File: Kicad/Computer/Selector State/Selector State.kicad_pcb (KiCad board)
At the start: 2 copper layers, 61 x 61 mm, 62 parts, among them IC1 FAN2558S38X, IC10 74LVC257AD,118, IC11 74LVC257AD,118, IC2 74LVC32APW,118, IC3 74LVC32APW,118, IC4 74LVC595APW, IC5 SN74ALVC08PWR, IC6 SN74ABT245BDBR, IC7 SN74ABT245BDBR, IC8 74ALVC04PW,118, IC9 74ALVC00PW,118, J1 Conn_01x02_Male, J10 Conn_01x02_Male, J11 Conn_01x10_Male, J12 Conn_01x02_Male, J2 Conn_01x12_Male, J3 Conn_01x02_Male, J4 Conn_01x02_Male, J5 Conn_01x12_Male, J6 Conn_01x02_Male, J7 Conn_01x02_Male, J8 Conn_01x10_Male, J9 Conn_01x02_Male

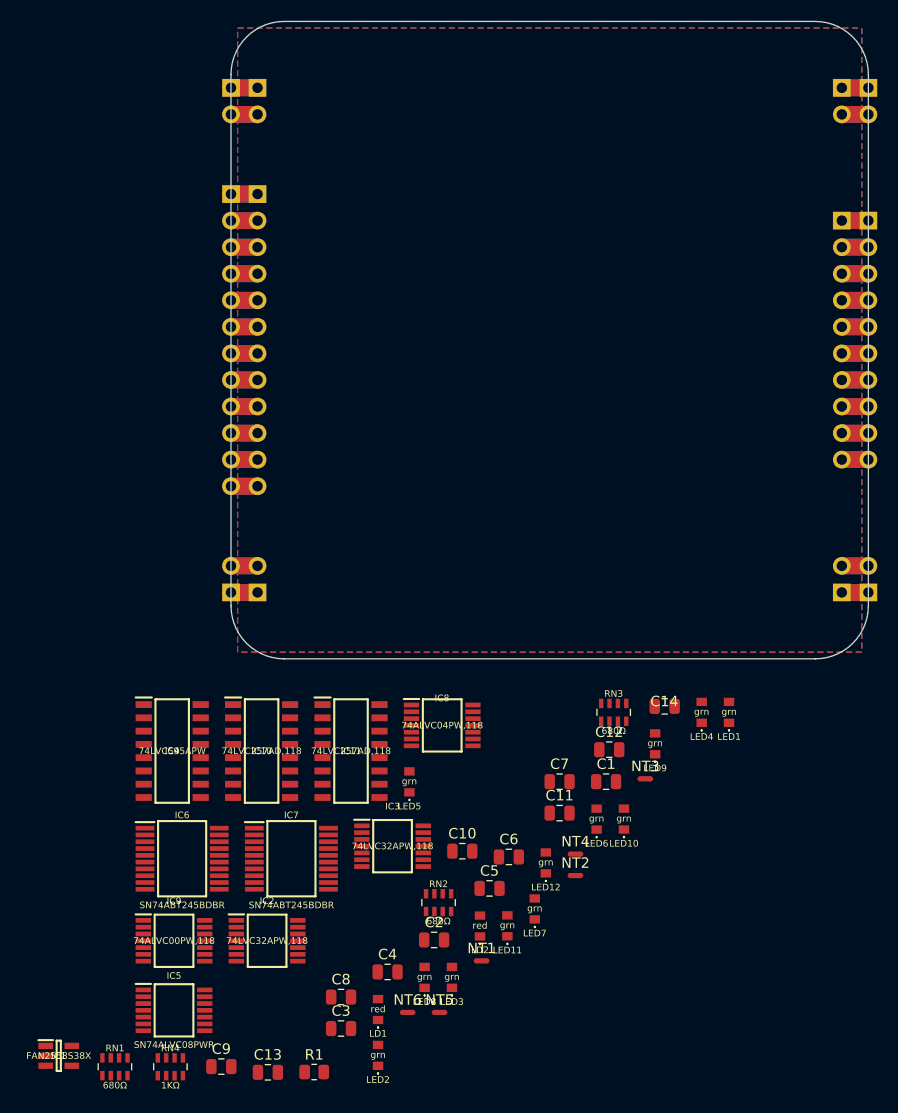
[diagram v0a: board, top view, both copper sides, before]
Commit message: Began routing Selector.
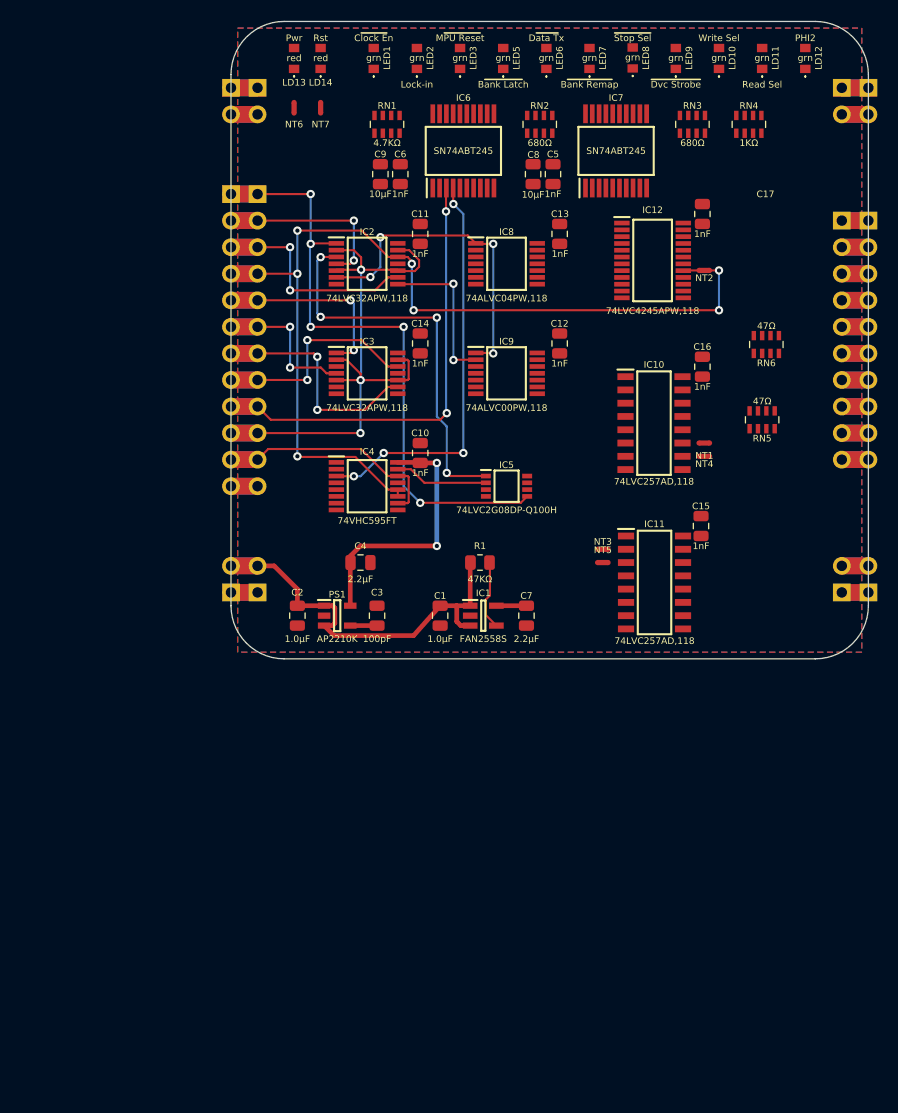
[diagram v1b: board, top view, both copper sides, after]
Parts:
- removed LD1, LD2: 150224SS73100, SamacSys_Parts:150224SS73100A
- removed LED10, LED11, LED12, LED4: 150224VS73100A, SamacSys_Parts:150224VS73100A
- added C15: C_Small, Capacitor_SMD:C_0805_2012Metric, F.Cu at (187.2, 85.1)
- added C16: C_Small, Capacitor_SMD:C_0805_2012Metric, F.Cu at (187.3, 69.8)
- added C17: C_Small, Capacitor_SMD:C_0805_2012Metric, F.Cu at (187.3, 55.2)
- added IC12: 74LVC4245APW,118, SamacSys_Parts:SOP65P640X110-24N, F.Cu at (182.6, 59.7)
- added LD10: 150224VS73100A, SamacSys_Parts:150224VS73100A, F.Cu at (188.9, 40.4)
- added LD11: 150224VS73100A, SamacSys_Parts:150224VS73100A, F.Cu at (193.0, 40.4)
- added LD12: 150224VS73100A, SamacSys_Parts:150224VS73100A, F.Cu at (197.2, 40.4)
- added LD13: 150224SS73100, SamacSys_Parts:150224SS73100A, F.Cu at (148.3, 40.4)
- added LD14: 150224SS73100, SamacSys_Parts:150224SS73100A, F.Cu at (150.8, 40.4)
- added NT7: NetTie_2, NetTie:NetTie-2_SMD_Pad0.5mm, F.Cu at (150.8, 45.1)
- added PS1: AP2210K-5.0TRG1, SamacSys_Parts:SOT95P282X130-5N, F.Cu at (152.4, 93.7)
- added RN5: CAY16-470J4LF, SamacSys_Parts:CAY16470J4LF, F.Cu at (193.0, 74.9)
- added RN6: CAY16-470J4LF, SamacSys_Parts:CAY16470J4LF, F.Cu at (193.4, 67.7)
- IC4: value 74LVC595APW -> 74VHC595FT; footprint SamacSys_Parts:SOIC127P600X175-16N -> SamacSys_Parts:SOP65P640X120-16N
- IC5: value SN74ALVC08PWR -> 74LVC2G08DP-Q100H; footprint SamacSys_Parts:SOP65P640X120-14N -> SamacSys_Parts:SOP65P400X110-8N
- IC6, IC7: value SN74ABT245BDBR -> SN74ABT245
- RN1: value CAY16-681J4LF -> CAY16-472J4LF
- moved RN4 105.8 mm to (191.8, 46.7)
- moved LED2 95.4 mm to (160.0, 40.4)
- moved RN1 93.8 mm to (157.2, 46.7)
- moved LED8 90.2 mm to (180.7, 40.3)
- moved LED3 87.9 mm to (164.1, 40.4)
- moved NT6 87.2 mm to (148.3, 45.1), turned to 90 degrees
- moved C9 86.7 mm to (156.5, 51.4), turned to 90 degrees
- moved C13 84.9 mm to (173.7, 57.1), turned to -90 degrees
- moved LED7 81.5 mm to (176.5, 40.4)
- moved C8 80.8 mm to (171.1, 51.4), turned to 90 degrees
- moved RN2 75.1 mm to (171.8, 46.7)
- moved IC7 74.5 mm to (179.1, 49.2), turned to 90 degrees
- moved LED6 72.9 mm to (172.4, 40.4)
- moved IC6 72.8 mm to (164.5, 49.2), turned to 90 degrees
- moved LED1 71.2 mm to (155.9, 40.4)
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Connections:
- net Net-(IC2-Pad6) renamed /Select 1 ^{AND} Enable
- net Net-(IC2-Pad8) renamed /Select 2 ^{AND} Enable
- net Net-(IC3-Pad11) renamed /Select 7 ^{AND} Enable
- net Net-(IC3-Pad3) renamed /Select 4 ^{AND} Enable
- net Net-(IC3-Pad6) renamed /Select 5 ^{AND} Enable
- net Net-(IC3-Pad8) renamed /Select 6 ^{AND} Enable
- C10 pad 2: VCC -> 5V
- C11 pad 2: VCC -> 3V
- C12 pad 2: VCC -> 3V
- C13 pad 2: VCC -> 3V
- C14 pad 2: VCC -> 3V
- C2 pad 2: VCC -> /Source 5V
- C3 pad 2: VCC -> Net-(C3-Pad2)
- C4 pad 2: VCC -> 5V
- C5 pad 2: VCC -> 5V
- C6 pad 2: VCC -> 5V
- C7 pad 2: VCC -> 3V
- C8 pad 2: VCC -> 5V
- C9 pad 2: VCC -> 5V
- IC1 pad 5: VCC -> 3V
- IC10 pad 16: VCC -> 3V
- IC10 pad 4: /~{Bank Latch} -> Net-(IC10-Pad4)
- IC10 pad 7: /~{Data Transmit} -> Net-(IC10-Pad7)
- IC10 pad 9: /~{Read Bank Remap} -> Net-(IC10-Pad9)
- IC11 pad 12: /~{PHI2} -> Net-(IC11-Pad12)
- IC11 pad 16: VCC -> 3V
- IC11 pad 4: /~{Device Strobe} -> Net-(IC11-Pad4)
- IC11 pad 7: /Write Selector -> Net-(IC11-Pad7)
- IC11 pad 9: /Read Selector -> Net-(IC11-Pad9)
- IC2 pad 11: unconnected-(IC2-Pad11) -> /Select 3 ^{AND} Enable
- IC2 pad 14: VCC -> 3V
- IC3 pad 14: VCC -> 3V
- IC4 pad 16: VCC -> 5V
- IC5 pad 3: /~{PHI2}_{1} -> /Read Selector_{2}
- IC5 pad 4: /~{Select 0} -> GND
- IC5 pad 5: /~{Select 4} -> /~{Select 0}
- IC5 pad 6: /Read Selector_{2} -> /~{Select 4}
- IC5 pad 7: GND -> /~{PHI2}_{1}
- IC5 pad 8: unconnected-(IC5-Pad8) -> 3V
- IC6 pad 1: VCC -> 5V
- IC6 pad 15: Net-(IC6-Pad15) -> unconnected-(IC6-Pad15)
- IC6 pad 2: unconnected-(IC6-Pad2) -> /~{Clock Enable}
- IC6 pad 20: VCC -> 5V
- IC6 pad 3: unconnected-(IC6-Pad3) -> /MPU Lock-in
- IC6 pad 4: unconnected-(IC6-Pad4) -> /Board ~{Reset}
- IC7 pad 1: VCC -> 5V
- IC7 pad 2: unconnected-(IC7-Pad2) -> /~{Bank Latch}
- IC7 pad 20: VCC -> 5V
- IC7 pad 3: unconnected-(IC7-Pad3) -> /~{Data Transmit}
- IC7 pad 4: unconnected-(IC7-Pad4) -> /~{Read Bank Remap}
- IC7 pad 5: unconnected-(IC7-Pad5) -> /~{Stop Selector}
- IC7 pad 6: unconnected-(IC7-Pad6) -> /~{Device Strobe}
- IC7 pad 7: unconnected-(IC7-Pad7) -> /Write Selector
- IC7 pad 8: unconnected-(IC7-Pad8) -> /Read Selector
- IC7 pad 9: unconnected-(IC7-Pad9) -> /~{PHI2}
- IC8 pad 14: VCC -> 3V
- IC9 pad 14: VCC -> 3V
- NT2 pad 2: /~{Stop Selector} -> Net-(IC12-Pad17)
- NT4 pad 1: VCC -> 3V
- NT6 pad 1: VCC -> 5V
- R1 pad 2: VCC -> /Source 5V
- RN1 pad 3: Net-(LED3-Pad1) -> unconnected-(RN1-Pad3)
- RN1 pad 4: Net-(LED4-Pad1) -> Net-(LED3-Pad1)
- RN1 pad 6: GND -> unconnected-(RN1-Pad6)
- RN4 pad 3: GND -> unconnected-(RN4-Pad3)
- RN4 pad 5: unconnected-(RN4-Pad5) -> Net-(LD14-Pad1)
- RN4 pad 6: Net-(LD2-Pad1) -> unconnected-(RN4-Pad6)
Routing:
- net /~{Select 3}: track 5.08 -> 92.9 mm, vias 0 -> 7
- net /~{Select 0}: track 5.08 -> 62.3 mm, vias 0 -> 5
- net /~{Clock Enable}: track 5.08 -> 58.9 mm, vias 0 -> 3
- net /MPU Lock-in: track 5.08 -> 45.5 mm, vias 0 -> 2
- net /Board ~{Reset}: track 5.08 -> 43.9 mm, vias 0 -> 4
- net /~{PHI2} Naked: track 0.00 -> 37.7 mm, vias 0 -> 4
- net /Source 5V: track 5.08 -> 40.4 mm
- net /Select 1 ^{AND} Enable: track 0.00 -> 30.8 mm, vias 0 -> 4
- net 5V: track 0.00 -> 25.1 mm, vias 0 -> 2
- net /~{Select 6}: track 5.08 -> 24.6 mm, vias 0 -> 2
- net /~{Reset}: track 5.08 -> 24.5 mm
- net /~{Select 7}: track 5.08 -> 23.4 mm, vias 0 -> 2
- net /~{Select 2}: track 5.08 -> 23.1 mm, vias 0 -> 2
- net /~{Select 4}: track 5.08 -> 20.6 mm, vias 0 -> 2
- net /~{Select 1}: track 5.08 -> 19.9 mm, vias 0 -> 2
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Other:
- board text added: "B~{ank Latc}h"
- board text added: "B~{ank Rema}p"
- board text added: "C~{lock E}n"
- board text added: "D~{ata T}x"
- board text added: "Lock-in"
- board text added: "M~{PU Rese}t"
- board text added: "PHI2"
- board text added: "Pwr"
- board text added: "Read Sel"
- board text added: "Rst"
- board text added: "Write Sel"
- board text added: "~{Dvc Strobe}"
- board text added: "~{Stop Sel}"

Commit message: Routed most Selector signals.
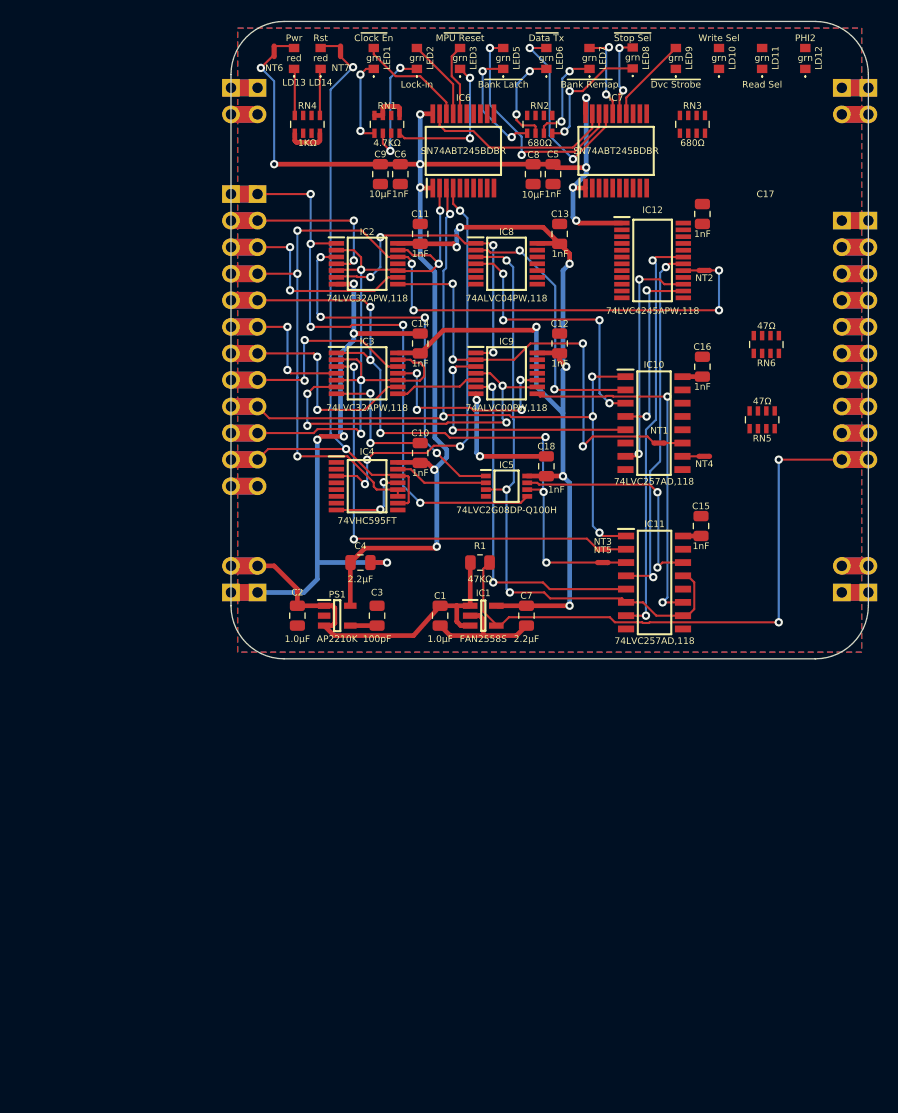
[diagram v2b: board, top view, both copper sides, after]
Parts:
- added C18: C_Small, Capacitor_SMD:C_0805_2012Metric, F.Cu at (172.4, 79.4)
- IC6, IC7: value SN74ABT245 -> SN74ABT245BDBR
- moved RN4 42.2 mm to (149.5, 46.7)
- moved NT6 5.72 mm to (146.4, 39.7)
- moved NT7 5.72 mm to (152.7, 39.7)
- moved NT1 4.31 mm to (183.2, 77.2), turned to 0 degrees
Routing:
- net GND: track 20.3 -> 127.7 mm, vias 0 -> 11
- net 5V: track 25.1 -> 123.3 mm, vias 2 -> 11
- net 3V: track 2.88 -> 97.3 mm, vias 0 -> 7
- net /Read Selector_{2}: track 0.00 -> 60.2 mm, vias 0 -> 3
- net /~{Power Error}: track 11.7 -> 61.1 mm, vias 0 -> 2
- net /~{Select 4}: track 20.6 -> 66.9 mm, vias 2 -> 6
- net /Select 4 ^{AND} Enable: track 0.00 -> 41.9 mm, vias 0 -> 2
- net /~{Reset}: track 24.5 -> 64.2 mm, vias 0 -> 2
- net Net-(IC11-Pad7): track 0.00 -> 39.5 mm, vias 0 -> 2
- net /MPU Lock-in: track 45.5 -> 81.2 mm, vias 2 -> 5
- net /Select 5 ^{AND} Enable: track 0.00 -> 35.4 mm, vias 0 -> 4
- net Net-(IC11-Pad4): track 0.00 -> 34.9 mm, vias 0 -> 2
- net /Read Selector_{1}: track 0.00 -> 34.4 mm, vias 0 -> 2
- net /Write Selector_{1}: track 0.00 -> 33.3 mm, vias 0 -> 2
- net /Select 2 ^{AND} Enable: track 14.8 -> 43.0 mm, vias 2 -> 4
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
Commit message: Finished routing Selector Clock.
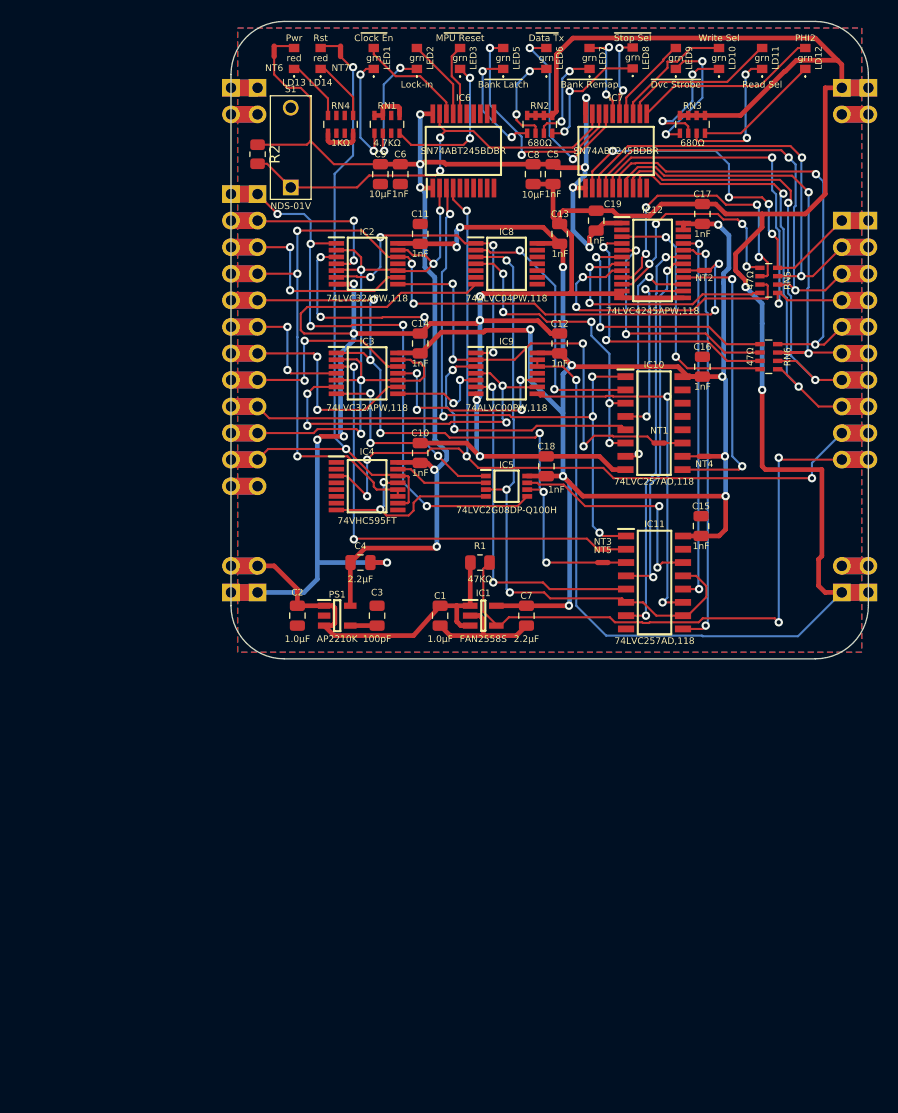
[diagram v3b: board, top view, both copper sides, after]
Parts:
- added C19: C_Small, Capacitor_SMD:C_0805_2012Metric, F.Cu at (177.2, 55.9)
- added R2: R_Small, Resistor_SMD:R_0805_2012Metric, F.Cu at (144.8, 49.5)
- added S1: NDS-01V, SamacSys_Parts:NDS01V, F.Cu at (148.0, 52.7)
- moved RN5 13.4 mm to (193.7, 61.6), turned to -90 degrees
- moved RN4 3.18 mm to (152.7, 46.7)
- moved RN6 1.19 mm to (193.7, 68.9), turned to -90 degrees
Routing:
- net GND: track 127.7 -> 433.9 mm, vias 11 -> 16
- net 3V: track 97.3 -> 165.7 mm, vias 7 -> 11
- net /~{Device Strobe}: track 5.08 -> 49.8 mm, vias 0 -> 2
- net /Write Selector: track 5.08 -> 49.4 mm, vias 0 -> 2
- net /Read Selector: track 5.08 -> 48.3 mm, vias 0 -> 2
- net /Board ~{Reset}: track 45.6 -> 88.4 mm, vias 4 -> 5
- net /~{PHI2}: track 5.08 -> 47.2 mm, vias 0 -> 2
- net /~{Data Transmit}: track 5.08 -> 46.0 mm, vias 0 -> 2
- net Net-(IC11-Pad9): track 0.00 -> 40.3 mm, vias 0 -> 2
- net /~{Read Bank Remap}: track 5.08 -> 45.1 mm, vias 0 -> 2
- net /~{Stop Selector}: track 5.08 -> 43.8 mm, vias 0 -> 2
- net /~{Bank Latch}: track 5.08 -> 42.8 mm, vias 0 -> 4
- net Net-(IC11-Pad12): track 0.00 -> 36.1 mm, vias 0 -> 2
- net Net-(IC10-Pad9): track 0.00 -> 28.9 mm, vias 0 -> 2
- net Net-(IC12-Pad8): track 0.00 -> 28.0 mm, vias 0 -> 2
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
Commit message: Optimise address decoding when in MPU Lock.
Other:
- board text added: "HCP65"
- board text added: "Selector State"
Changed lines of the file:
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@@
     )
   )
+  (gr_line (start 188.9125 91.1225) (end 197.8025 91.1225) (layer "F.SilkS") (width 0.2))
   (gr_line (start 142.239996 41.91) (end 142.24 92.71) (layer "Edge.Cuts") (width 0.1))
   (gr_line (start 198.12 97.79) (end 147.32 97.79) (layer "Edge.Cuts") (width 0.1))
@@
     (effects (font (size 0.635 0.635) (thickness 0.15)))
   )
+  (gr_text "Selector State" (at 193.3575 92.075) (layer "F.SilkS")
+    (effects (font (size 1 1) (thickness 0.2)))
+  )
   (gr_text "Write Sel" (at 188.9125 38.4175) (layer "F.SilkS")
     (effects (font (size 0.635 0.635) (thickness 0.15)))
@@
   (gr_text "PHI2" (at 197.1675 38.4175) (layer "F.SilkS")
     (effects (font (size 0.635 0.635) (thickness 0.15)))
+  )
+  (gr_text "HCP65" (at 193.3575 89.535) (layer "F.SilkS")
+    (effects (font (size 2.3 2.3) (thickness 0.5)))
   )
   (gr_text "D~{ata T}x" (at 172.4025 38.4175) (layer "F.SilkS")
@@
     )
   )
+  (group "" (id d046cc50-7477-404f-9327-6ede228ef48f)
+    (members
+      0387aa58-0e1b-4ad1-85ae-f05b9779ef31
+      526ba924-7715-4488-8555-57c756f340fc
+      8135eabd-97ad-478f-9192-3cd57fde404f
+    )
+  )
